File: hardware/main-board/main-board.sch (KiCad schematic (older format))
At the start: 76 parts, among them J1 USB_B_Micro, J2 STDC14, J3 Display Connector, J4 Conn_01x02, SW1 SW_Push, SW2 SW_Push, SW3 SW_Push, SW4 SW_Push, SW5 SW_Detect, U1 TSL2591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

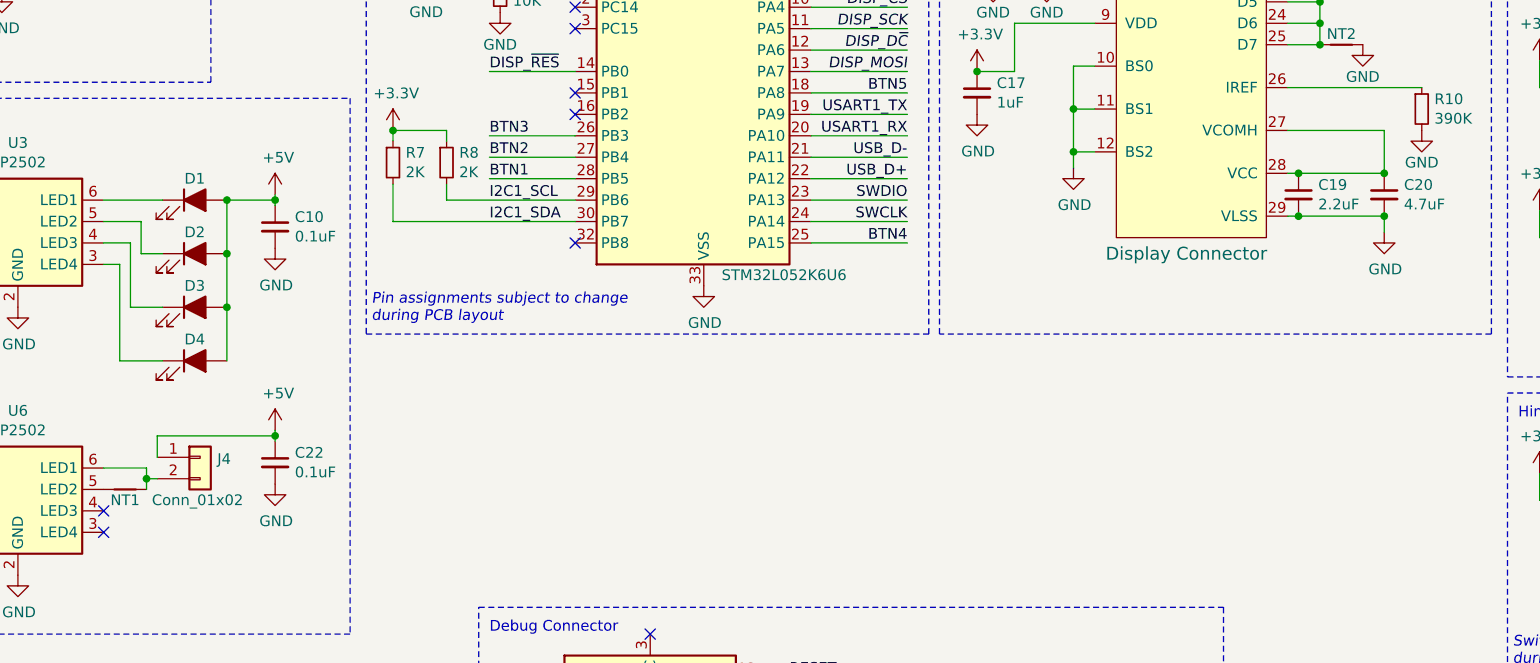
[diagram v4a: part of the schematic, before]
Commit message: Updated component data and fixed a display connector issue
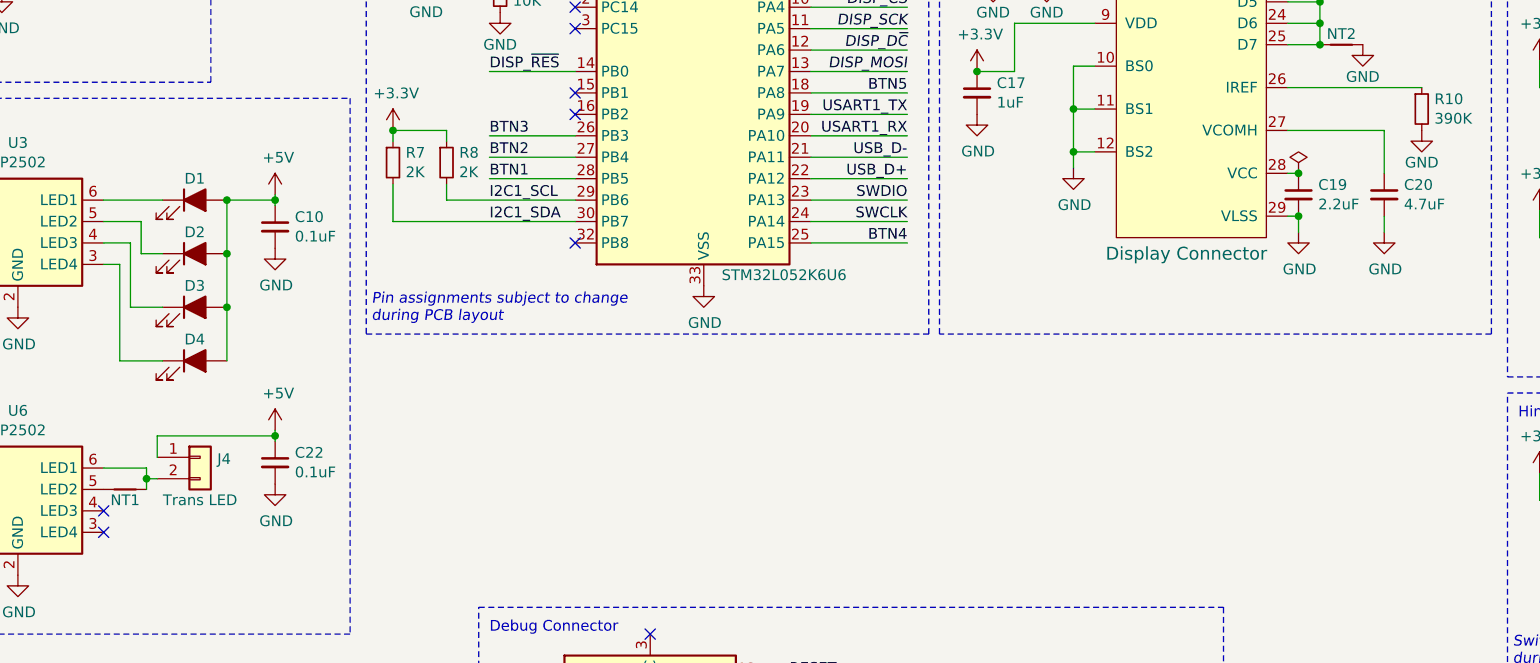
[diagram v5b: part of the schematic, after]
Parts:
- C14, C15, C16, C17: footprint (none) -> Capacitor_SMD:C_0603_1608Metric; Description (none) -> CAP CER 1UF 25V X7R 0603; Manufacturer (none) -> Samsung Electro-Mechanics; Manufacturer PN (none) -> CL10B105KA8NNNC; Supplier (none) -> Digi-Key; Supplier PN (none) -> 1276-1184-1-ND
- C19: footprint (none) -> Capacitor_SMD:C_0603_1608Metric; Description (none) -> CAP CER 2.2UF 10V X7R 0603; Manufacturer (none) -> Samsung Electro-Mechanics; Manufacturer PN (none) -> CL10B225KP8NNNC; Supplier (none) -> Digi-Key; Supplier PN (none) -> 1276-1134-1-ND
- C20: footprint (none) -> Capacitor_SMD:C_0603_1608Metric; Description (none) -> CAP CER 4.7UF 16V X5R 0603; Manufacturer (none) -> TDK Corporation; Manufacturer PN (none) -> C1608X5R1C475K080AC; Supplier (none) -> Digi-Key; Supplier PN (none) -> 445-7478-1-ND
- J3: Description (none) -> CONN FFC TOP 30POS 0.50MM R/A; Manufacturer (none) -> EastRising; Manufacturer PN (none) -> ER-CON30HT-1; Supplier (none) -> BuyDisplay
- J4: footprint (none) -> Connector_JST:JST_PH_B2B-PH-K_1x02_P2.00mm_Vertical; Description (none) -> CONN HEADER VERT 2POS 2MM; Manufacturer (none) -> JST Sales America Inc.; Manufacturer PN (none) -> B2B-PH-K-S(LF)(SN); Supplier (none) -> Digi-Key; Supplier PN (none) -> 455-1704-ND; User Label (none) -> Trans LED
- NT1, NT2: footprint (none) -> NetTie:NetTie-2_SMD_Pad0.5mm
- R10: footprint (none) -> Resistor_SMD:R_0603_1608Metric; Description (none) -> RES SMD 390K OHM 1% 1/10W 0603; Manufacturer (none) -> Vishay Dale; Manufacturer PN (none) -> CRCW0603390KFKEAC; Supplier (none) -> Digi-Key; Supplier PN (none) -> 541-5379-1-ND
- TP2: footprint TestPoint:TestPoint_Keystone_5005-5009_Compact -> TestPoint:TestPoint_Pad_D2.0mm; Description PC TEST POINT COMPACT BLACK -> (none); Manufacturer Keystone Electronics -> (none); Manufacturer PN 5006 -> (none); Supplier Digi-Key -> (none); Supplier PN 36-5006-ND -> (none); User Label (none) -> 3.3V
- U1: Description (none) -> SENSOR OPT AMBIENT 6DFN; Manufacturer (none) -> ams; Manufacturer PN (none) -> TSL25911FN; Supplier (none) -> Mouser; Supplier PN (none) -> 985-TSL25911FN
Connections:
- net at C20.1, J3.27 (VCOMH): no longer C19.1, J3.28 (VCC)
- new net: C19.1, J3.28 (VCC)
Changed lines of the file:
@@
 F 0 "TP2" H 4983 7322 50  0000 L CNN
 F 1 "3.3V" H 4983 7277 50  0001 L CNN
-F 2 "TestPoint:TestPoint_Keystone_5005-5009_Compact" H 5125 7250 50  0001 C CNN
-F 3 "http://www.keyelco.com/product-pdf.cfm?p=1314" H 5125 7250 50  0001 C CNN
-F 4 "PC TEST POINT COMPACT BLACK" H 4925 7250 50  0001 C CNN "Description"
-F 5 "Keystone Electronics" H 4925 7250 50  0001 C CNN "Manufacturer"
-F 6 "5006" H 4925 7250 50  0001 C CNN "Manufacturer PN"
-F 7 "Digi-Key" H 4925 7250 50  0001 C CNN "Supplier"
-F 8 "36-5006-ND" H 4925 7250 50  0001 C CNN "Supplier PN"
+F 2 "TestPoint:TestPoint_Pad_D2.0mm" H 5125 7250 50  0001 C CNN
+F 3 "~" H 5125 7250 50  0001 C CNN
+F 4 "3.3V" H 4925 7250 50  0001 C CNN "User Label"
 	1    4925 7250
 	1    0    0    -1
@@
 F 2 "lib_fp:AMS_TSL2591" H 1250 1125 50  0001 C CNN
 F 3 "http://ams.com/documents/20143/36005/TSL2591_DS000338_5-00.pdf" H 2000 1925 50  0001 C CNN
+F 4 "SENSOR OPT AMBIENT 6DFN" H 1250 1625 50  0001 C CNN "Description"
+F 5 "ams" H 1250 1625 50  0001 C CNN "Manufacturer"
+F 6 "TSL25911FN" H 1250 1625 50  0001 C CNN "Manufacturer PN"
+F 7 "Mouser" H 1250 1625 50  0001 C CNN "Supplier"
+F 8 "985-TSL25911FN" H 1250 1625 50  0001 C CNN "Supplier PN"
 	1    1250 1625
 	1    0    0    -1
@@
 P 2175 4200
 F 0 "J4" H 2255 4192 50  0000 L CNN
-F 1 "Conn_01x02" H 1950 4000 50  0000 L CNN
-F 2 "" H 2175 4200 50  0001 C CNN
-F 3 "~" H 2175 4200 50  0001 C CNN
+F 1 "Conn_01x02" H 1950 4000 50  0001 L CNN
+F 2 "Connector_JST:JST_PH_B2B-PH-K_1x02_P2.00mm_Vertical" H 2175 4200 50  0001 C CNN
+F 3 "http://www.jst-mfg.com/product/pdf/eng/ePH.pdf" H 2175 4200 50  0001 C CNN
+F 4 "Trans LED" H 2175 4000 50  0000 C CNN "User Label"
+F 5 "CONN HEADER VERT 2POS 2MM" H 2175 4200 50  0001 C CNN "Description"
+F 6 "JST Sales America Inc." H 2175 4200 50  0001 C CNN "Manufacturer"
+F 7 "B2B-PH-K-S(LF)(SN)" H 2175 4200 50  0001 C CNN "Manufacturer PN"
+F 8 "Digi-Key" H 2175 4200 50  0001 C CNN "Supplier"
+F 9 "455-1704-ND" H 2175 4200 50  0001 C CNN "Supplier PN"
 	1    2175 4200
 	1    0    0    -1
@@
 F 0 "C14" H 6142 1121 50  0000 L CNN
 F 1 "1uF" H 6142 1030 50  0000 L CNN
-F 2 "" H 6050 1075 50  0001 C CNN
-F 3 "~" H 6050 1075 50  0001 C CNN
+F 2 "Capacitor_SMD:C_0603_1608Metric" H 6050 1075 50  0001 C CNN
+F 3 "https://media.digikey.com/pdf/Data%20Sheets/Samsung%20PDFs/CL10B105KA8NNNC_char.pdf" H 6050 1075 50  0001 C CNN
+F 4 "CAP CER 1UF 25V X7R 0603" H 6050 1075 50  0001 C CNN "Description"
+F 5 "Samsung Electro-Mechanics" H 6050 1075 50  0001 C CNN "Manufacturer"
+F 6 "CL10B105KA8NNNC" H 6050 1075 50  0001 C CNN "Manufacturer PN"
+F 7 "Digi-Key" H 6050 1075 50  0001 C CNN "Supplier"
+F 8 "1276-1184-1-ND" H 6050 1075 50  0001 C CNN "Supplier PN"
 	1    6050 1075
 	1    0    0    -1
@@
 F 0 "C15" H 6142 1521 50  0000 L CNN
 F 1 "1uF" H 6142 1430 50  0000 L CNN
-F 2 "" H 6050 1475 50  0001 C CNN
-F 3 "~" H 6050 1475 50  0001 C CNN
+F 2 "Capacitor_SMD:C_0603_1608Metric" H 6050 1475 50  0001 C CNN
+F 3 "https://media.digikey.com/pdf/Data%20Sheets/Samsung%20PDFs/CL10B105KA8NNNC_char.pdf" H 6050 1475 50  0001 C CNN
+F 4 "CAP CER 1UF 25V X7R 0603" H 6050 1475 50  0001 C CNN "Description"
+F 5 "Samsung Electro-Mechanics" H 6050 1475 50  0001 C CNN "Manufacturer"
+F 6 "CL10B105KA8NNNC" H 6050 1475 50  0001 C CNN "Manufacturer PN"
+F 7 "Digi-Key" H 6050 1475 50  0001 C CNN "Supplier"
+F 8 "1276-1184-1-ND" H 6050 1475 50  0001 C CNN "Supplier PN"
 	1    6050 1475
 	1    0    0    -1
@@
 F 1 "Display Connector" H 6400 800 60  0000 L CNN
 F 2 "lib_fp:ER-CON30HT-1" H 6978 1919 60  0001 L CNN
-F 3 "" H 7250 3725 60  0000 C CNN
+F 3 "https://www.buydisplay.com/download/connector/ER-CON30HT-1.pdf" H 7250 3725 60  0001 C CNN
+F 4 "CONN FFC TOP 30POS 0.50MM R/A" H 6800 2025 50  0001 C CNN "Description"
+F 5 "EastRising" H 6800 2025 50  0001 C CNN "Manufacturer"
+F 6 "ER-CON30HT-1" H 6800 2025 50  0001 C CNN "Manufacturer PN"
+F 7 "BuyDisplay" H 6800 2025 50  0001 C CNN "Supplier"
 	1    6800 2025
 	1    0    0    -1
@@
 F 0 "C16" H 5967 1921 50  0000 L CNN
 F 1 "1uF" H 5967 1830 50  0000 L CNN
-F 2 "" H 5875 1875 50  0001 C CNN
-F 3 "~" H 5875 1875 50  0001 C CNN
+F 2 "Capacitor_SMD:C_0603_1608Metric" H 5875 1875 50  0001 C CNN
+F 3 "https://media.digikey.com/pdf/Data%20Sheets/Samsung%20PDFs/CL10B105KA8NNNC_char.pdf" H 5875 1875 50  0001 C CNN
+F 4 "CAP CER 1UF 25V X7R 0603" H 5875 1875 50  0001 C CNN "Description"
+F 5 "Samsung Electro-Mechanics" H 5875 1875 50  0001 C CNN "Manufacturer"
+F 6 "CL10B105KA8NNNC" H 5875 1875 50  0001 C CNN "Manufacturer PN"
+F 7 "Digi-Key" H 5875 1875 50  0001 C CNN "Supplier"
+F 8 "1276-1184-1-ND" H 5875 1875 50  0001 C CNN "Supplier PN"
 	1    5875 1875
 	1    0    0    -1
@@
 F 0 "C17" H 5892 2546 50  0000 L CNN
 F 1 "1uF" H 5892 2455 50  0000 L CNN
-F 2 "" H 5800 2500 50  0001 C CNN
-F 3 "~" H 5800 2500 50  0001 C CNN
+F 2 "Capacitor_SMD:C_0603_1608Metric" H 5800 2500 50  0001 C CNN
+F 3 "https://media.digikey.com/pdf/Data%20Sheets/Samsung%20PDFs/CL10B105KA8NNNC_char.pdf" H 5800 2500 50  0001 C CNN
+F 4 "CAP CER 1UF 25V X7R 0603" H 5800 2500 50  0001 C CNN "Description"
+F 5 "Samsung Electro-Mechanics" H 5800 2500 50  0001 C CNN "Manufacturer"
+F 6 "CL10B105KA8NNNC" H 5800 2500 50  0001 C CNN "Manufacturer PN"
+F 7 "Digi-Key" H 5800 2500 50  0001 C CNN "Supplier"
+F 8 "1276-1184-1-ND" H 5800 2500 50  0001 C CNN "Supplier PN"
 	1    5800 2500
 	1    0    0    -1
@@
 F 0 "R10" H 7934 2621 50  0000 L CNN
 F 1 "390K" H 7934 2530 50  0000 L CNN
-F 2 "" H 7875 2575 50  0001 C CNN
-F 3 "~" H 7875 2575 50  0001 C CNN
+F 2 "Resistor_SMD:R_0603_1608Metric" H 7875 2575 50  0001 C CNN
+F 3 "https://www.vishay.com/docs/28773/crcwce3.pdf" H 7875 2575 50  0001 C CNN
+F 4 "RES SMD 390K OHM 1% 1/10W 0603" H 7875 2575 50  0001 C CNN "Description"
+F 5 "Vishay Dale" H 7875 2575 50  0001 C CNN "Manufacturer"
+F 6 "CRCW0603390KFKEAC" H 7875 2575 50  0001 C CNN "Manufacturer PN"
+F 7 "Digi-Key" H 7875 2575 50  0001 C CNN "Supplier"
+F 8 "541-5379-1-ND" H 7875 2575 50  0001 C CNN "Supplier PN"
 	1    7875 2575
 	1    0    0    -1
@@
 F 0 "C20" H 7792 3021 50  0000 L CNN
 F 1 "4.7uF" H 7792 2930 50  0000 L CNN
-F 2 "" H 7700 2975 50  0001 C CNN
-F 3 "~" H 7700 2975 50  0001 C CNN
+F 2 "Capacitor_SMD:C_0603_1608Metric" H 7700 2975 50  0001 C CNN
+F 3 "https://product.tdk.com/info/en/catalog/datasheets/mlcc_commercial_general_en.pdf" H 7700 2975 50  0001 C CNN
+F 4 "CAP CER 4.7UF 16V X5R 0603" H 7700 2975 50  0001 C CNN "Description"
+F 5 "TDK Corporation" H 7700 2975 50  0001 C CNN "Manufacturer"
+F 6 "C1608X5R1C475K080AC" H 7700 2975 50  0001 C CNN "Manufacturer PN"
+F 7 "Digi-Key" H 7700 2975 50  0001 C CNN "Supplier"
+F 8 "445-7478-1-ND" H 7700 2975 50  0001 C CNN "Supplier PN"
 	1    7700 2975
 	1    0    0    -1
@@
 F 0 "C19" H 7392 3021 50  0000 L CNN
 F 1 "2.2uF" H 7392 2930 50  0000 L CNN
-F 2 "" H 7300 2975 50  0001 C CNN
-F 3 "~" H 7300 2975 50  0001 C CNN
+F 2 "Capacitor_SMD:C_0603_1608Metric" H 7300 2975 50  0001 C CNN
+F 3 "http://www.samsungsem.com/kr/support/product-search/mlcc/CL10B225KP8NNNC.jsp" H 7300 2975 50  0001 C CNN
+F 4 "CAP CER 2.2UF 10V X7R 0603" H 7300 2975 50  0001 C CNN "Description"
+F 5 "Samsung Electro-Mechanics" H 7300 2975 50  0001 C CNN "Manufacturer"
+F 6 "CL10B225KP8NNNC" H 7300 2975 50  0001 C CNN "Manufacturer PN"
+F 7 "Digi-Key" H 7300 2975 50  0001 C CNN "Supplier"
+F 8 "1276-1134-1-ND" H 7300 2975 50  0001 C CNN "Supplier PN"
 	1    7300 2975
 	1    0    0    -1
@@
 Wire Wire Line
 	7250 3075 7300 3075
-Connection ~ 7300 2875
 Wire Wire Line
 	7700 2675 7250 2675
-Connection ~ 7700 2875
-Connection ~ 7700 3075
-Connection ~ 7300 3075
 Wire Wire Line
 	6350 1775 5875 1775
 Connection ~ 5875 1775
-Wire Wire Line
-	7300 2875 7700 2875
-Wire Wire Line
-	7300 3075 7700 3075
 Wire Wire Line
 	7700 3075 7700 3150
@@
 F 0 "NT1" H 1825 4300 50  0000 C CNN
 F 1 "Net-Tie_2" H 1825 4440 50  0001 C CNN
-F 2 "" H 1825 4350 50  0001 C CNN
+F 2 "NetTie:NetTie-2_SMD_Pad0.5mm" H 1825 4350 50  0001 C CNN
 F 3 "~" H 1825 4350 50  0001 C CNN
 	1    1825 4350
@@
 F 0 "NT2" H 7500 2325 50  0000 C CNN
 F 1 "Net-Tie_2" H 7500 2365 50  0001 C CNN
-F 2 "" H 7500 2275 50  0001 C CNN
+F 2 "NetTie:NetTie-2_SMD_Pad0.5mm" H 7500 2275 50  0001 C CNN
 F 3 "~" H 7500 2275 50  0001 C CNN
 	1    7500 2275
@@
 Text Notes 8300 5175 0    50   Italic 0
 Switch choice subject to change\nduring mechanical design
+$Comp
+L power:GND #PWR0119
+U 1 1 60BE6FE8
+P 7300 3150
+F 0 "#PWR0119" H 7300 2900 50  0001 C CNN
+F 1 "GND" H 7305 2977 50  0000 C CNN
+F 2 "" H 7300 3150 50  0001 C CNN
+F 3 "" H 7300 3150 50  0001 C CNN
+	1    7300 3150
+	1    0    0    -1
+$EndComp
+Wire Wire Line
+	7300 3075 7300 3150
+Connection ~ 7300 3075
+$Comp
+L power:PWR_FLAG #FLG0103
+U 1 1 60BF6E7F
+P 7300 2875
+F 0 "#FLG0103" H 7300 2950 50  0001 C CNN
+F 1 "PWR_FLAG" H 7300 3048 50  0001 C CNN
+F 2 "" H 7300 2875 50  0001 C CNN
+F 3 "~" H 7300 2875 50  0001 C CNN
+	1    7300 2875
+	1    0    0    -1
+$EndComp
+Connection ~ 7300 2875
 $EndSCHEMATC
